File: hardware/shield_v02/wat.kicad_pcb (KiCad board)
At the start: 2 copper layers, 101.8 x 85.9 mm, 42 parts, among them P1 PINZA_1, P102 CAUDAL_1, P103 V_IN, P106 18b20, P109 LCD_I2C, P110 ARD_DI_06, P111 ARD_ALI_04, P2 PINZA_7, P3 PINZA_2, P4 PINZA_8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

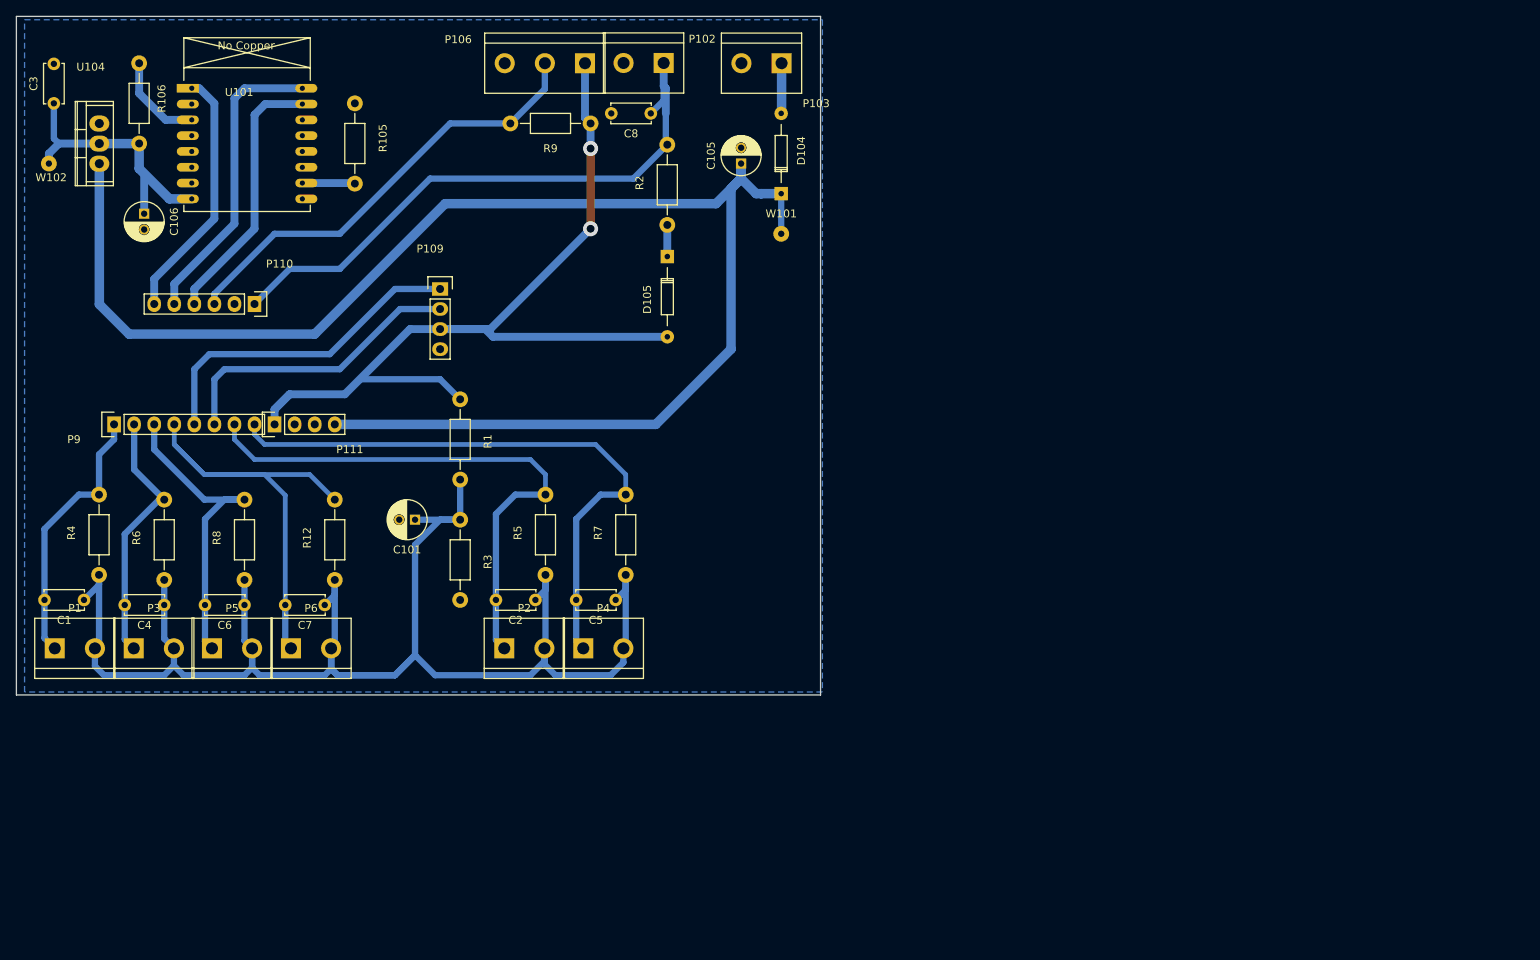
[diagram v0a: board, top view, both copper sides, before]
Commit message: pcb cambio de valores de resistencias de carga
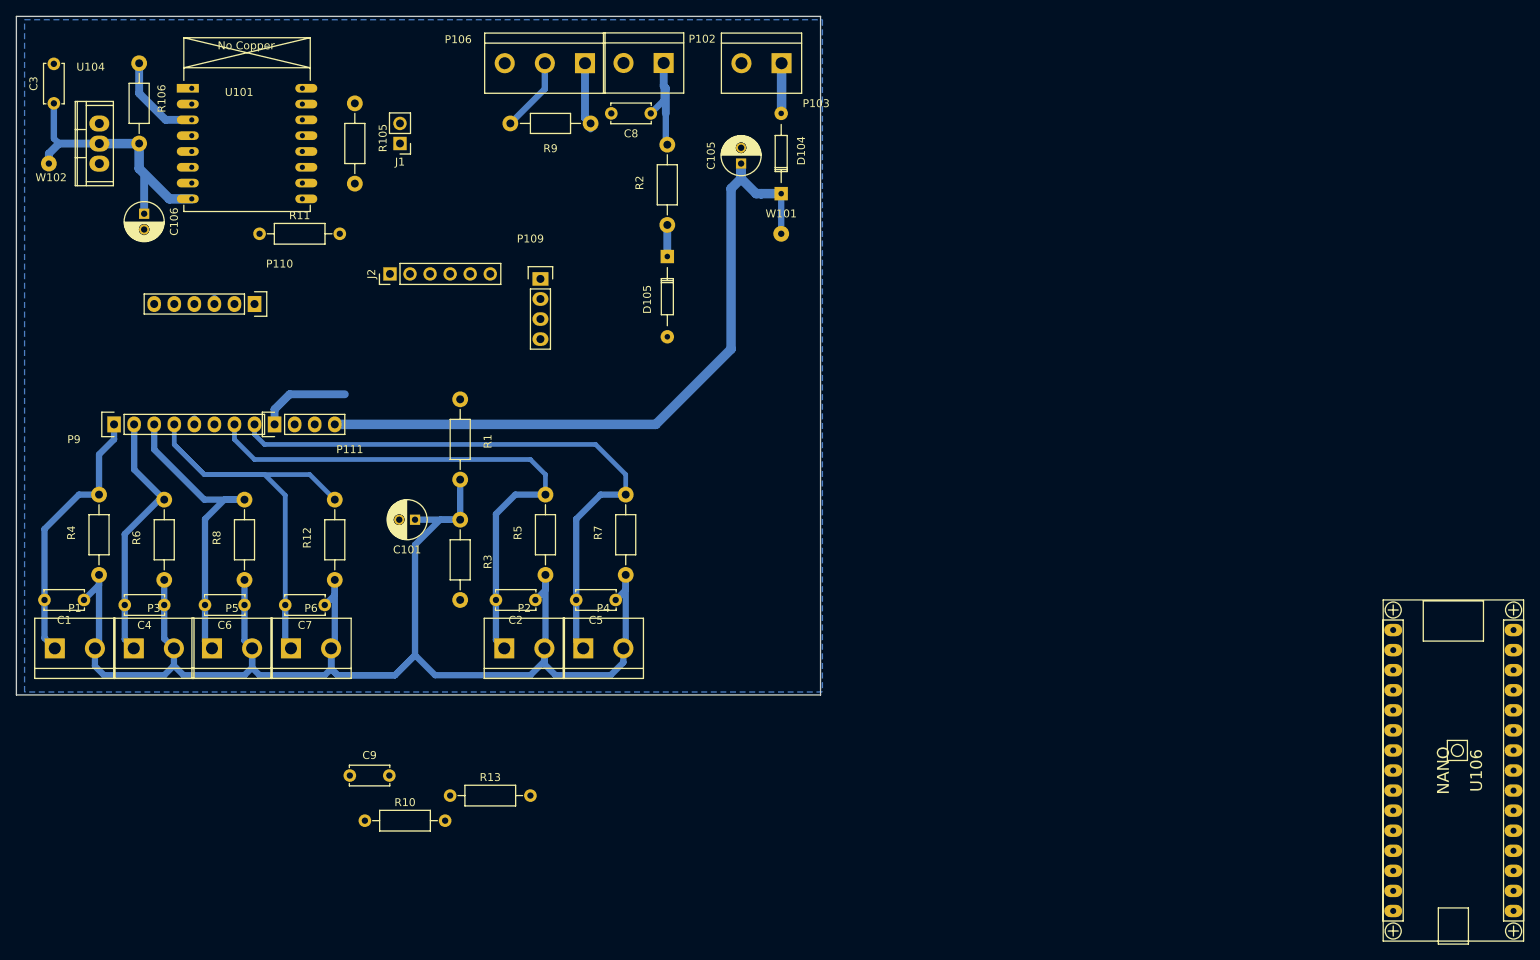
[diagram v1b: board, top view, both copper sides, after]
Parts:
- added C9: 100nF, Capacitors_THT:C_Disc_D5.0mm_W2.5mm_P5.00mm, F.Cu at (130.8, 139.7)
- added J1: GPIO_0, Pin_Headers:Pin_Header_Straight_1x02_Pitch2.54mm, F.Cu at (137.2, 59.7)
- added J2: FTDI, Pin_Headers:Pin_Header_Straight_1x06_Pitch2.54mm, F.Cu at (135.9, 76.2)
- added R10: 10K, Resistors_THT:R_Axial_DIN0207_L6.3mm_D2.5mm_P10.16mm_Horizontal, F.Cu at (132.7, 145.4)
- added R11: 4K7, Resistors_THT:R_Axial_DIN0207_L6.3mm_D2.5mm_P10.16mm_Horizontal, F.Cu at (119.4, 71.1)
- added R13: 10K, Resistors_THT:R_Axial_DIN0207_L6.3mm_D2.5mm_P10.16mm_Horizontal, F.Cu at (143.5, 142.2)
- added U106: NANO, oscar_libreria_huellas:arduino_nano, F.Cu at (270.5, 139.1)
- R12, R8: value R20 -> R18
- R4, R6: value 10k -> R18
- R5, R7: value R10 -> R18
- moved P109 12.8 mm to (154.9, 76.8)
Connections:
- net /e_tx renamed /esp_tx
- P110 pad 4: /e_rx -> /n_d5_tx
- U101 pad 15: /e_rx -> /esp_rx
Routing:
- net /Var_8V: track 205.7 -> 96.9 mm
- net /Vpc_5V: track 133.2 -> 34.4 mm, vias 2 -> 0
- net /caudal_1: track 78.2 -> 17.6 mm
- net /18b20: track 57.7 -> 10.1 mm
- net /sda: track 42.9 -> 0.64 mm
- net /esp_tx: track 38.3 -> 0.00 mm
- net /scl: track 38.0 -> 0.00 mm
- net /e_rx: track 33.7 -> 0.00 mm
- net /e_rst: track 32.2 -> 0.00 mm
- net /e_g15: track 6.67 -> 0.10 mm
